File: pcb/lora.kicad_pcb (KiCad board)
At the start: 4 copper layers, 80.5 x 45 mm, 51 parts, among them J11 Conn_Coaxial, J2 Humidity, J3 Temp, J5 Temp, J6 VDD, J7 GPS, J8 SIM800, J9 I2C, Q1 AO3401A, Q2 AO3401A, Q3 AO3401A, Q5 AO3401A, SW1 RESET, SW2 PJ, U2 ESP32-WROOM-32D, U3 2460, U4 RFM95W-868S2, Y1 Crystal

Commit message: figured all GPIOs out
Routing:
- added copper zone on In1.Cu, net GND
- added copper zone on In2.Cu, net VBATT
- removed copper zone on In1.Cu_GND, net GND
- removed copper zone on In2.Cu_VDD, net VBATT
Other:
- net class Default removed

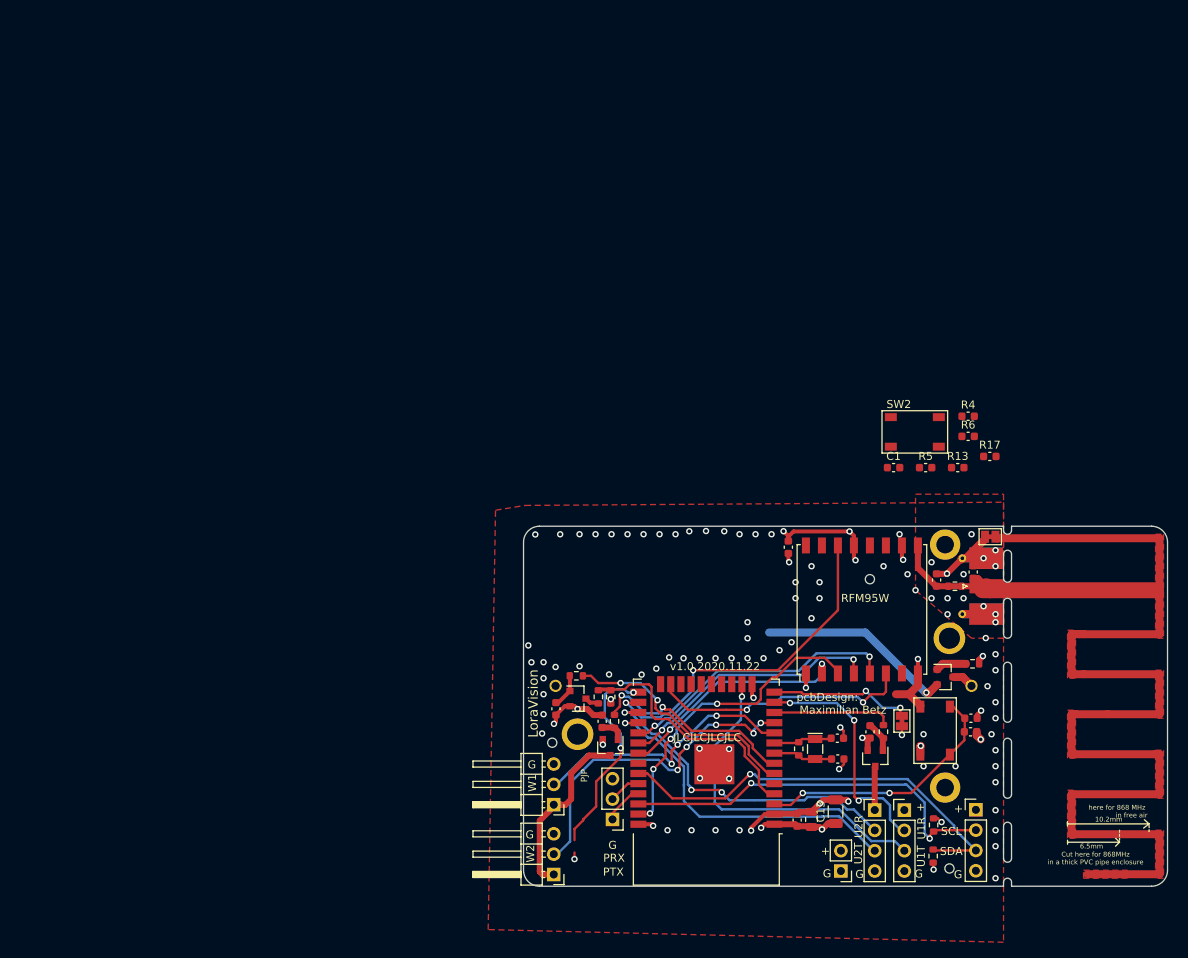
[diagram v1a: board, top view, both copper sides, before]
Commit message: updated layout
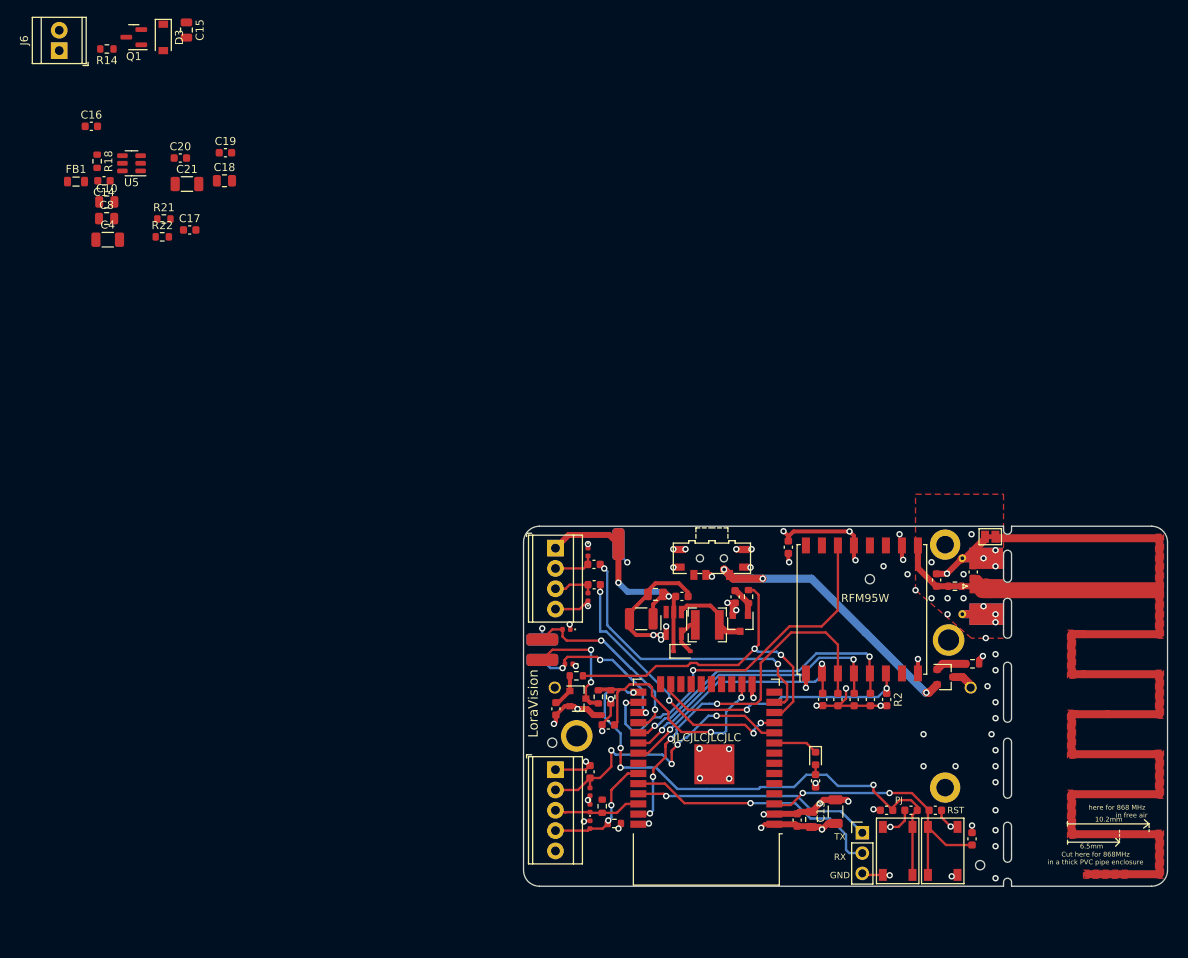
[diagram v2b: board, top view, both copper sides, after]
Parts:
- removed J8: SIM800, Connector_PinHeader_2.54mm:PinHeader_1x04_P2.54mm_Vertical
- removed J9: I2C, Connector_PinHeader_2.54mm:PinHeader_1x04_P2.54mm_Vertical
- removed JP2: Bridged, Jumper:SolderJumper-2_P1.3mm_Bridged_Pad1.0x1.5mm
- removed Y1: Crystal, Crystal:Crystal_SMD_MicroCrystal_CC7V-T1A-2Pin_3.2x1.5mm
- added C14: 100n, Capacitor_SMD:C_0603_1608Metric, F.Cu at (117.6, 48.8)
- added C15: 10u, Capacitor_SMD:C_0805_2012Metric, F.Cu at (127.9, 30.0)
- added C16: 100n, Capacitor_SMD:C_0603_1608Metric, F.Cu at (116.0, 42.0)
- added C17: 100p, Capacitor_SMD:C_0603_1608Metric, F.Cu at (128.3, 55.0)
- added C18: 10u, Capacitor_SMD:C_0805_2012Metric, F.Cu at (132.6, 48.8)
- added C19: 1u, Capacitor_SMD:C_0603_1608Metric, F.Cu at (132.7, 45.3)
- added C2: 100n, Capacitor_SMD:C_0603_1608Metric, F.Cu at (180.6, 116.8)
- added C20: 100n, Capacitor_SMD:C_0603_1608Metric, F.Cu at (127.1, 46.0)
- added C21: 47u, Capacitor_SMD:C_1206_3216Metric, F.Cu at (127.9, 49.2)
- added C22: 2u2, Capacitor_SMD:C_0805_2012Metric, F.Cu at (186.5, 100.5)
- added C23: 100n, Capacitor_SMD:C_0603_1608Metric, F.Cu at (189.8, 100.8)
- added C3: 47u, Capacitor_SMD:C_1210_3225Metric, F.Cu at (184.7, 103.6)
- added C4: 47u, Capacitor_SMD:C_1206_3216Metric, F.Cu at (118.0, 56.2)
- added D1: LED_Small, LED_SMD:LED_0603_1608Metric, F.Cu at (206.5, 121.0)
- added D10: D_TVS, Diode_SMD:D_0402_1005Metric, F.Cu at (178.3, 129.3)
- added D2: D_Schottky, Diode_SMD:D_SOD-323, F.Cu at (189.8, 107.6)
- added D3: D_MM1Z15, Diode_SMD:D_SOD-123, F.Cu at (125.0, 30.9)
- added D4: D_TVS, Diode_SMD:D_0402_1005Metric, F.Cu at (178.3, 125.2)
- added D5: D_TVS, Diode_SMD:D_0402_1005Metric, F.Cu at (178.3, 127.3)
- added D6: D_TVS, Diode_SMD:D_0402_1005Metric, F.Cu at (178.1, 100.8)
- added D7: D_TVS, Diode_SMD:D_0402_1005Metric, F.Cu at (178.1, 95.2)
- added D8: D_TVS, Diode_SMD:D_0402_1005Metric, F.Cu at (175.4, 104.9)
- added D9: D_TVS, Diode_SMD:D_0402_1005Metric, F.Cu at (175.7, 109.2)
- added FB1: Ferrite, Inductor_SMD:L_0805_2012Metric, F.Cu at (114.1, 48.9)
- added J1: Conn_01x04, TerminalBlock_TE-Connectivity:TerminalBlock_TE_282834-4_1x04_P2.54mm_Horizontal, F.Cu at (174.0, 94.7)
- added L1: 47u, OWN_Parts_:L_SWPA4018S, F.Cu at (193.0, 104.3)
- added R18: 100k, Resistor_SMD:R_0603_1608Metric, F.Cu at (116.7, 46.4)
- added R20: 4k7, Capacitor_SMD:C_0603_1608Metric, F.Cu at (178.3, 122.7)
- added R21: 62k, Resistor_SMD:R_0603_1608Metric, F.Cu at (125.0, 53.6)
- added R22: 20k, Resistor_SMD:R_0603_1608Metric, F.Cu at (124.8, 55.8)
- added R23: 1k, Capacitor_SMD:C_0603_1608Metric, F.Cu at (178.8, 99.3)
- added R24: 1k, Capacitor_SMD:C_0603_1608Metric, F.Cu at (178.8, 96.8)
- added SW3: K3-1296S-E1, OWN_Parts_:K3-1296S-E1, F.Cu at (193.5, 96.0)
- added U1: ME2108C50M5G, Package_TO_SOT_SMD:SOT-23-5_HandSoldering, F.Cu at (188.8, 104.1)
- added U5: SCT2400, Package_TO_SOT_SMD:TSOT-23-6, F.Cu at (121.0, 46.6)
- C10: value 18p -> 2u2; footprint Capacitor_SMD:C_0603_1608Metric -> Capacitor_SMD:C_0805_2012Metric
- C8: value 18p -> 10u; footprint Capacitor_SMD:C_0603_1608Metric -> Capacitor_SMD:C_0805_2012Metric
- J2: value Humidity -> 5V; footprint Connector_PinHeader_2.54mm:PinHeader_1x03_P2.54mm_Horizontal -> OWN_Parts_:pcb_edge_2_1
- J3: value Temp -> Conn_01x05; footprint Connector_PinHeader_2.54mm:PinHeader_1x03_P2.54mm_Horizontal -> TerminalBlock_TE-Connectivity:TerminalBlock_TE_282834-5_1x05_P2.54mm_Horizontal
- J6: footprint Connector_PinHeader_2.54mm:PinHeader_1x02_P2.54mm_Vertical -> TerminalBlock_TE-Connectivity:TerminalBlock_TE_282834-2_1x02_P2.54mm_Horizontal
- J7: value GPS -> UART; footprint Connector_PinHeader_2.54mm:PinHeader_1x04_P2.54mm_Vertical -> OWN_Parts_:pcb_edge_2_2
- R1: value 10k -> 1k
- R14: value dnp -> 100k
- R15, R16: value 2k2 -> 4k7
- R2: value 100 -> 10k; footprint Resistor_SMD:R_0603_1608Metric -> Capacitor_SMD:C_0603_1608Metric
- moved J6 141.6 mm to (112.0, 32.5), turned to 90 degrees
- moved R14 123.0 mm to (117.9, 32.3), turned to 180 degrees
- moved C8 113.6 mm to (117.9, 53.5), turned to 0 degrees
- moved C10 113.3 mm to (117.9, 51.5)
- moved Q1 106.9 mm to (121.3, 30.9), turned to 180 degrees
- moved SW2 52.3 mm to (216.9, 132.6), turned to 90 degrees
- moved R4 50.3 mm to (215.4, 127.5), turned to 180 degrees
- moved J7 46.1 mm to (172.3, 107.4)
- moved C1 42.9 mm to (218.4, 127.5)
- moved J2 42.1 mm to (181.9, 94.2), turned to 90 degrees
- moved R16 41.5 mm to (179.8, 127.0)
- moved R15 40.1 mm to (181.4, 129.2), turned to 180 degrees
- moved R6 36.7 mm to (209.3, 113.7), turned to 90 degrees
- moved R2 34.1 mm to (215.4, 113.7)
- moved R17 33.9 mm to (213.4, 113.7), turned to 90 degrees
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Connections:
- C10 pad 1: 32K_XN -> Net-(C10-Pad1)
- C13 pad 2: VBATT -> VDD
- C6 pad 2: VBATT -> VDD
- C7 pad 2: VBATT -> VDD
- C8 pad 1: GND -> Net-(C10-Pad1)
- C8 pad 2: 32K_XP -> GND
- C9 pad 2: VBATT -> VDD
- J2 pad 1: Net-(J2-Pad1) -> BUCK_5V
- J2 pad 2: ONEWIRE2_DATA -> GND
- J3 pad 1: Net-(J2-Pad1) -> VDD
- J3 pad 3: GND -> I2C_SCL
- J6 pad 2: VBATT -> VSUPPLY_IN
- J7 pad 1: Net-(J7-Pad1) -> VDD_SWITCHED
- Q1 pad 1: Net-(Q1-Pad1) -> Net-(D3-Pad2)
- Q1 pad 2: VBATT -> VSUPPLY
- Q1 pad 3: Net-(J2-Pad1) -> VSUPPLY_IN
- Q2 pad 2: VBATT -> VDD
- Q2 pad 3: Net-(Q2-Pad3) -> VDD_SWITCHED
- Q3 pad 2: VBATT -> VDD
- Q3 pad 3: Net-(J7-Pad1) -> 5V_EN
- R1 pad 1: VBATT -> VDD
- R1 pad 2: Net-(Q1-Pad1) -> Net-(D1-Pad2)
- R10 pad 1: VDD_SENSE_MOSFET_SWITCH -> POWER_EN
- R11 pad 1: VBATT -> VDD
- R12 pad 1: GPS_MOSFET_SWITCH -> POWER_EN
- R13 pad 1: VBATT -> VDD
- R14 pad 1: 32K_XP -> GND
- R14 pad 2: 32K_XN -> Net-(D3-Pad2)
- R15 pad 1: VBATT -> VDD
- R16 pad 1: VBATT -> VDD
- R17 pad 1: VBATT -> VDD
- R2 pad 1: VDD_SENSOR_MOSFET_SWITCH -> RFM_RST
- R2 pad 2: Net-(Q1-Pad1) -> VDD
- R3 pad 2: VBATT -> VDD
- R4 pad 2: VBATT -> VDD
- R5 pad 1: VBATT -> VDD
- R6 pad 1: VBATT -> VDD
- R7 pad 2: Net-(Q2-Pad3) -> VDD_SWITCHED
- R9 pad 1: VBATT -> VDD
- U2 pad 11: ONEWIRE2_DATA -> EXT_ADC_SENSE2
- U2 pad 12: GPS_MOSFET_SWITCH -> POWER_EN
- U2 pad 13: UART1_RX -> EXT_ADC_SENSE
- U2 pad 14: Net-(JP2-Pad1) -> unconnected-(U2-Pad14)
- U2 pad 16: UART1_TX -> VDD_SENSE
- U2 pad 17: Net-(U2-Pad17) -> unconnected-(U2-Pad17)
- U2 pad 18: Net-(U2-Pad18) -> unconnected-(U2-Pad18)
- U2 pad 19: Net-(U2-Pad19) -> unconnected-(U2-Pad19)
- U2 pad 2: VBATT -> VDD
- U2 pad 20: Net-(U2-Pad20) -> unconnected-(U2-Pad20)
- U2 pad 21: Net-(U2-Pad21) -> unconnected-(U2-Pad21)
- U2 pad 22: Net-(U2-Pad22) -> unconnected-(U2-Pad22)
- U2 pad 24: Net-(U2-Pad24) -> unconnected-(U2-Pad24)
- U2 pad 32: Net-(U2-Pad32) -> unconnected-(U2-Pad32)
- U2 pad 4: VDD_SENSE -> unconnected-(U2-Pad4)
- U2 pad 5: Net-(U2-Pad5) -> unconnected-(U2-Pad5)
- U2 pad 6: VDD_SENSE_MOSFET_SWITCH -> unconnected-(U2-Pad6)
- U2 pad 7: VDD_SENSOR_MOSFET_SWITCH -> unconnected-(U2-Pad7)
- U2 pad 8: 32K_XP -> unconnected-(U2-Pad8)
- U2 pad 9: 32K_XN -> LED_SIGNAL
- U3 pad 1: Net-(Q5-Pad3) -> Net-(JP2-Pad1)
- U4 pad 11: Net-(U4-Pad11) -> unconnected-(U4-Pad11)
- U4 pad 12: Net-(U4-Pad12) -> unconnected-(U4-Pad12)
- U4 pad 13: VBATT -> VDD
- U4 pad 15: Net-(U4-Pad15) -> unconnected-(U4-Pad15)
- U4 pad 16: Net-(U4-Pad16) -> unconnected-(U4-Pad16)
- U4 pad 7: Net-(U4-Pad7) -> unconnected-(U4-Pad7)
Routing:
- net VDD: track 0.00 -> 58.4 mm, vias 0 -> 19
- net POWER_EN: track 0.00 -> 44.6 mm, vias 0 -> 2
- net UART1_TX: track 42.4 -> 0.00 mm, vias 1 -> 0
- net ONEWIRE2_DATA: track 42.0 -> 0.00 mm, vias 5 -> 0
- net GND: track 54.9 -> 95.2 mm, vias 101 -> 72
- net PRG_JP: track 26.0 -> 65.8 mm, vias 2 -> 4
- net I2C_SCL: track 49.9 -> 11.0 mm, vias 2 -> 0
- net I2C_SDA: track 55.1 -> 16.3 mm, vias 1 -> 2
- net EXT_ADC_SENSE: track 0.00 -> 38.0 mm, vias 0 -> 2
- net EXT_ADC_SENSE2: track 0.00 -> 34.7 mm, vias 0 -> 4
- net BUCK_5V: track 0.00 -> 33.1 mm, vias 0 -> 2
- net VBATT: track 70.0 -> 38.7 mm, vias 16 -> 3
- net VDD_SENSE_MOSFET_SWITCH: track 30.9 -> 0.00 mm, vias 2 -> 0
- net UART1_RX: track 29.8 -> 0.00 mm, vias 3 -> 0
- net PRG_RX: track 4.03 -> 32.7 mm, vias 0 -> 1
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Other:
- outline, holes or cut-outs redrawn
- board text added: "GND"
- board text added: "PJ"
- board text added: "RST"
- board text added: "RX"
- board text added: "TX"
- board text removed: "+"
- board text removed: "-"
- board text removed: "G"
- board text removed: "PJP"
- board text removed: "PRX"
- board text removed: "PTX"
- board text removed: "SCL"
- board text removed: "SDA"
- board text removed: "U1R"
- board text removed: "U1T"
- board text removed: "U2R"
- board text removed: "U2T"
- board text removed: "W1"
- board text removed: "W2"

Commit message: updated layout
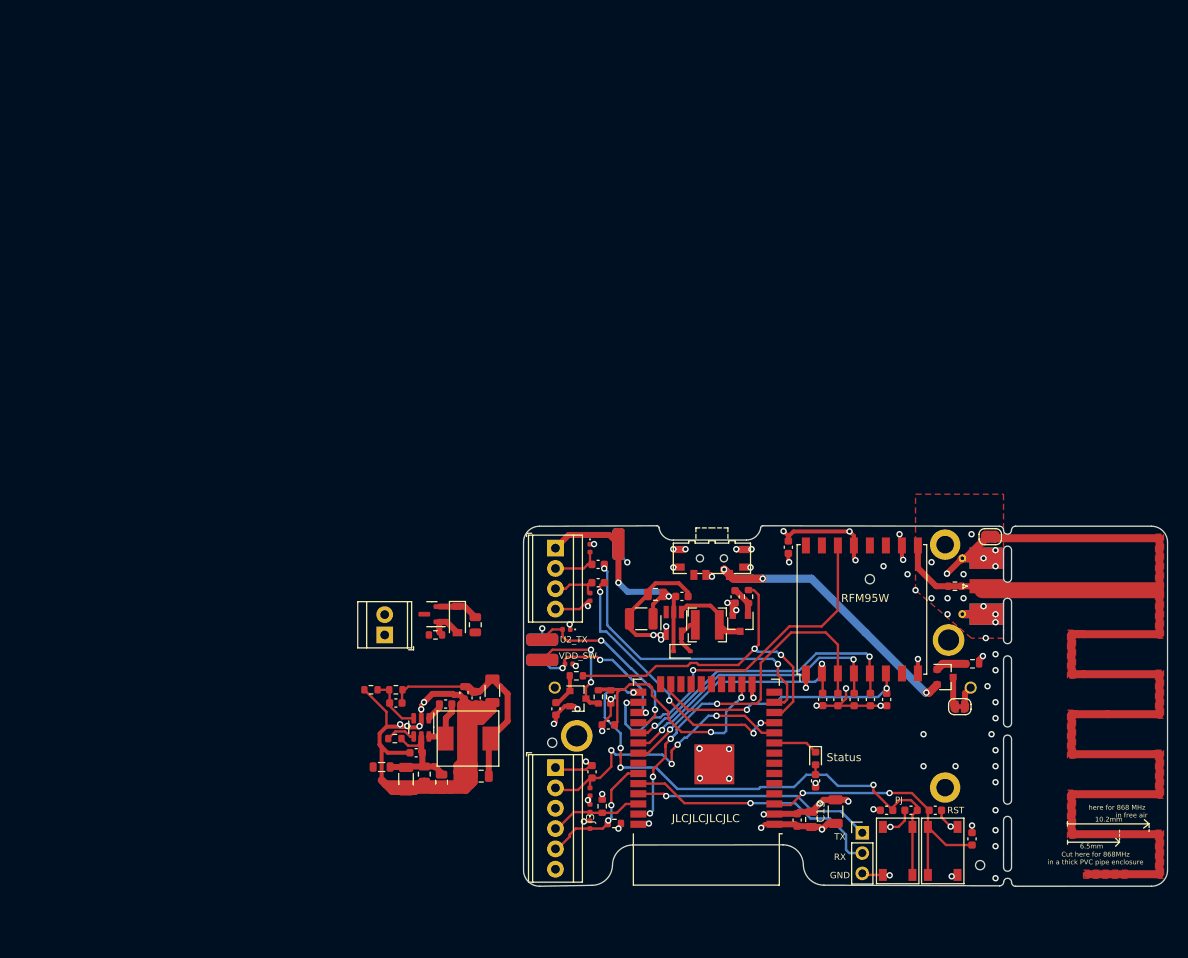
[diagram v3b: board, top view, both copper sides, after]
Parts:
- removed C11, C12: dnp, Capacitor_SMD:C_0603_1608Metric
- added JP2: ISense, Jumper:SolderJumper-2_P1.3mm_Bridged_RoundedPad1.0x1.5mm, F.Cu at (224.5, 114.6)
- added L3: 15u, OWN_Parts_:SLO0630H, F.Cu at (163.1, 118.5)
- J3: value Conn_01x05 -> Conn_01x06; footprint TerminalBlock_TE-Connectivity:TerminalBlock_TE_282834-5_1x05_P2.54mm_Horizontal -> TerminalBlock_TE-Connectivity:TerminalBlock_TE_282834-6_1x06_P2.54mm_Horizontal
- JP1: footprint Jumper:SolderJumper-2_P1.3mm_Bridged_Pad1.0x1.5mm -> OWN_Parts_:jumperhidden
- moved C16 84.7 mm to (160.3, 114.2), turned to 180 degrees
- moved R14 84.0 mm to (159.0, 105.6), turned to 0 degrees
- moved C10 83.7 mm to (159.8, 124.0), turned to -90 degrees
- moved J6 83.6 mm to (152.6, 105.6)
- moved C15 82.7 mm to (164.0, 104.3)
- moved FB1 82.5 mm to (152.3, 122.1)
- moved D3 81.5 mm to (161.7, 103.7)
- moved C14 81.5 mm to (156.6, 120.3), turned to 0 degrees
- moved R18 81.2 mm to (153.9, 118.5), turned to 0 degrees
- moved Q1 81.2 mm to (158.5, 103.0)
- moved C18 81.0 mm to (164.7, 123.2), turned to 180 degrees
- moved C8 80.0 mm to (157.6, 123.0), turned to -90 degrees
- moved U5 79.3 mm to (157.2, 117.1), turned to -90 degrees
- moved C4 77.1 mm to (155.3, 123.6), turned to -90 degrees
- moved C20 75.7 mm to (162.5, 112.8), turned to 90 degrees
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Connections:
- J3 pad 3: I2C_SCL -> GND
- J3 pad 4: I2C_SDA -> I2C_SCL
- J3 pad 5: GND -> I2C_SDA
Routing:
- net GND: track 95.2 -> 205.3 mm, vias 72 -> 77
- net 3V3EXT: track 0.00 -> 27.4 mm
- net Net-(C10-Pad1): track 0.00 -> 14.0 mm
- net Net-(C17-Pad2): track 0.00 -> 7.14 mm
- net Net-(C16-Pad1): track 0.00 -> 6.86 mm
- net VSUPPLY: track 0.00 -> 5.08 mm
- net Net-(D3-Pad2): track 0.00 -> 4.61 mm
- net Net-(R18-Pad1): track 0.00 -> 3.81 mm
- net Net-(J11-Pad1): track 174.8 -> 172.1 mm
- net VDD: track 58.4 -> 55.7 mm, vias 19 -> 20
- net Net-(JP2-Pad1): track 0.00 -> 2.67 mm
- net Net-(C16-Pad2): track 0.00 -> 2.33 mm
- net SPI_SCK: track 37.8 -> 36.0 mm
- net Net-(JP2-Pad2): track 2.75 -> 3.78 mm
- net UART2_TX: track 24.7 -> 23.8 mm
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- added copper zone on In2.Cu, net VDD
- removed copper zone on In2.Cu, net VBATT
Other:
- board size 80.5 x 45 mm -> 80.5 x 45.1 mm
- board text added: "AcreLink"
- board text added: "BATT"
- board text added: "Status"
- board text added: "U2_TX"
- board text added: "VDD_SW"
- board text added: "V_EXT/OFF"
- board text removed: "LoraVision"

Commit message: updated some text
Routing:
- net GND: vias 77 -> 75
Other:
- outline, holes or cut-outs redrawn
- board text added: "v2.0 2022.01.29"
- board text removed: "v1.0 2020.11.22"
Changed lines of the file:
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@@
   (gr_line (start 178.543949 136.887949) (end 172 137) (layer "Edge.Cuts") (width 0.05))
   (gr_arc (start 207.554102 136.869898) (mid 205.757869 136.140785) (end 204.978 134.366) (layer "Edge.Cuts") (width 0.05))
-  (gr_circle (center 213.294 98.62) (end 213.87 98.62) (layer "Edge.Cuts") (width 0.05) (fill none))
+  (gr_circle (center 205.74 102.108) (end 206.316 102.108) (layer "Edge.Cuts") (width 0.05) (fill none))
   (gr_line (start 202.438 131.826) (end 183.660051 131.844051) (layer "Edge.Cuts") (width 0.05))
   (gr_arc (start 231.49921 137.00399) (mid 231.145927 136.854689) (end 231 136.5) (layer "Edge.Cuts") (width 0.05))
@@
     (effects (font (size 1 1) (thickness 0.15)) (justify mirror))
   )
-  (gr_text "pcbDesign:" (at 207.97 113.37) (layer "B.SilkS")
-    (effects (font (size 1 1) (thickness 0.15)) (justify mirror))
-  )
-  (gr_text "AcreLink" (at 181.102 106.172 90) (layer "B.SilkS")
-    (effects (font (size 1.2 1.2) (thickness 0.2)) (justify mirror))
+  (gr_text "pcbDesign:" (at 222.25 132.842) (layer "B.SilkS")
+    (effects (font (size 1 1) (thickness 0.15)) (justify mirror))
+  )
+  (gr_text "AcreLink" (at 215.646 94.742) (layer "B.SilkS")
+    (effects (font (size 1.4 1.4) (thickness 0.25)) (justify mirror))
   )
   (gr_text "BATT" (at 196.342 97.028 90) (layer "B.SilkS")
     (effects (font (size 1 1) (thickness 0.15)) (justify mirror))
   )
-  (gr_text "Maximilian Betz" (at 209.93 114.97) (layer "B.SilkS")
+  (gr_text "Maximilian Betz" (at 220.218 134.62) (layer "B.SilkS")
     (effects (font (size 1 1) (thickness 0.2)) (justify mirror))
   )
-  (gr_text "LifePo4 or Lithium-Thionyl-Chlorid\n3.6V MAX!" (at 200.406 123.444) (layer "B.SilkS")
-    (effects (font (size 1 1) (thickness 0.15)) (justify mirror))
-  )
-  (gr_text "v1.0 2020.11.22" (at 193.93 109.53) (layer "B.SilkS")
+  (gr_text "LifePo4 or Lithium-Thionyl-Chlorid\n3.6V MAX!" (at 200.406 123.698) (layer "B.SilkS")
+    (effects (font (size 1 1) (thickness 0.15)) (justify mirror))
+  )
+  (gr_text "v2.0 2022.01.29" (at 213.614 97.79) (layer "B.SilkS")
     (effects (font (size 1 1) (thickness 0.15)) (justify mirror))
   )
@@
   (via (at 215.773 135.636) (size 0.8) (drill 0.45) (layers "F.Cu" "B.Cu") (net 1))
   (via (at 229 127.5) (size 0.8) (drill 0.45) (layers "F.Cu" "B.Cu") (net 1))
-  (via (at 215 97) (size 0.8) (drill 0.45) (layers "F.Cu" "B.Cu") (net 1))
   (via (at 226 93) (size 0.8) (drill 0.45) (layers "F.Cu" "B.Cu") (net 1))
   (via (at 220 118) (size 0.8) (drill 0.45) (layers "F.Cu" "B.Cu") (net 1))
@@
   (via (at 195.7 119.85) (size 0.8) (drill 0.45) (layers "F.Cu" "B.Cu") (net 1))
   (via (at 203.2 96.5) (size 0.8) (drill 0.45) (layers "F.Cu" "B.Cu") (net 1))
-  (via (at 218 98) (size 0.8) (drill 0.45) (layers "F.Cu" "B.Cu") (net 1))
   (via (at 222.93025 97.93025) (size 0.8) (drill 0.45) (layers "F.Cu" "B.Cu") (net 1))
   (segment (start 181.864 94.234) (end 181.864 95.406625) (width 0.3) (layer "B.Cu") (net 1))
